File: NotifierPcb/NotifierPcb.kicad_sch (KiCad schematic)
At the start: 29 parts, among them IC1 CD4067BEE4, IC2 ESP32-WROOM-32E__8MB_, J1 RC_433_MHZ_RF, J2 UART_Conn, J3 Power_Conn, U1 HT75xx-1-SOT89

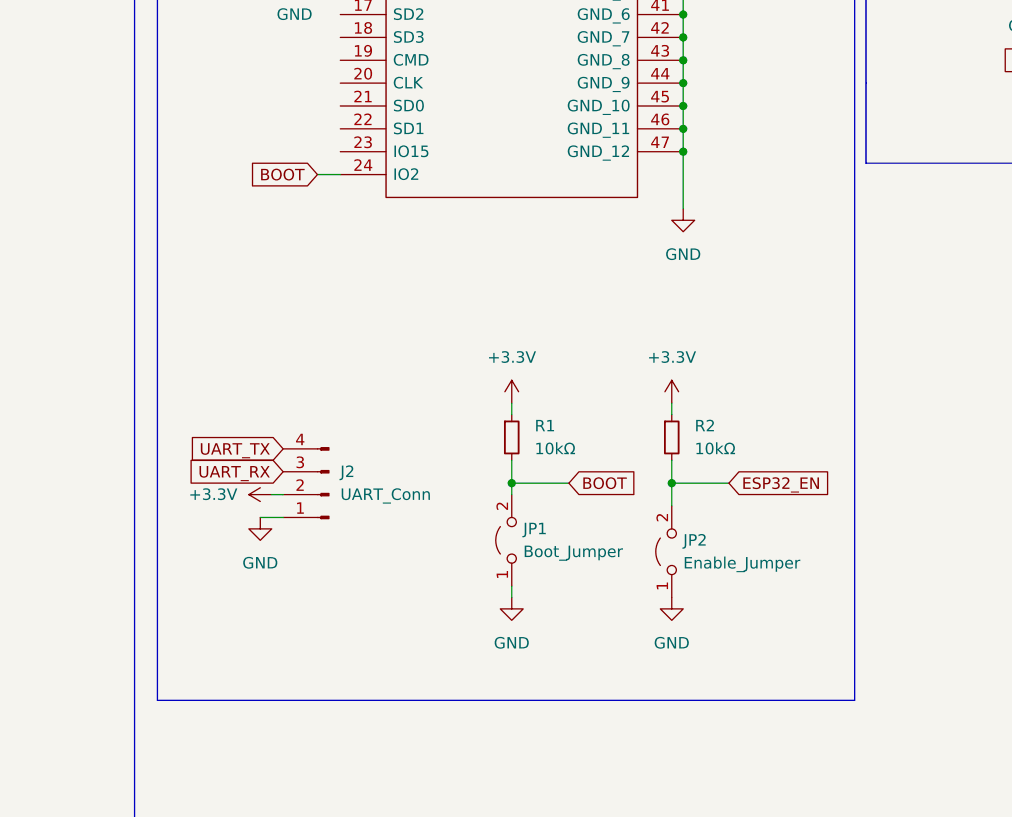
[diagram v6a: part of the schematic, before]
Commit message: fixing strapping pins for download mode
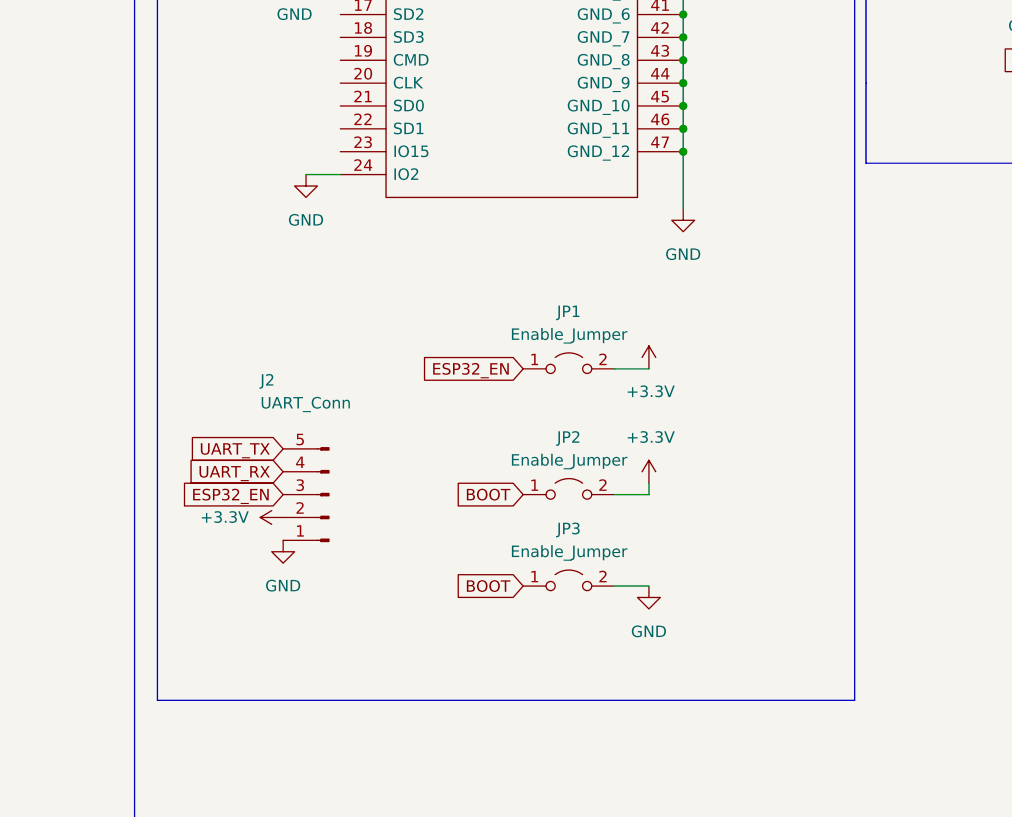
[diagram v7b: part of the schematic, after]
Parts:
- removed J2: UART_Conn, Connector_PinHeader_2.54mm:PinHeader_1x04_P2.54mm_Vertical, symbol Connector:Conn_01x04_Male
- removed JP1: Boot_Jumper, Connector_PinHeader_2.54mm:PinHeader_1x02_P2.54mm_Vertical, symbol Jumper:Jumper_2_Open
- removed R1, R2: 10kΩ, Resistor_THT:R_Axial_DIN0204_L3.6mm_D1.6mm_P2.54mm_Vertical, symbol Device:R_Small
- added J2: UART_Conn, symbol Connector:Conn_01x05_Male
- added JP2, JP3: Enable_Jumper, Connector_PinHeader_2.54mm:PinHeader_1x02_P2.54mm_Vertical, symbol Jumper:Jumper_2_Open
- renumbered JP2 to JP1
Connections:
- net +3.3V: now also JP1.2 (B), J2.2 (Pin_2), JP2.2 (B)
- net BOOT: now also JP2.1 (A), JP3.1 (A); no longer IC2.24 (IO2)
- net ESP32_EN: now also JP1.1 (A), J2.3 (Pin_3); no longer JP1.2 (B)
- net GND: now also IC2.24 (IO2), J2.1 (Pin_1), JP3.2 (B); no longer JP1.1 (A)
- net UART_RX: now also J2.4 (Pin_4)
- net UART_TX: now also J2.5 (Pin_5)
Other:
- moved on the sheet: JP1

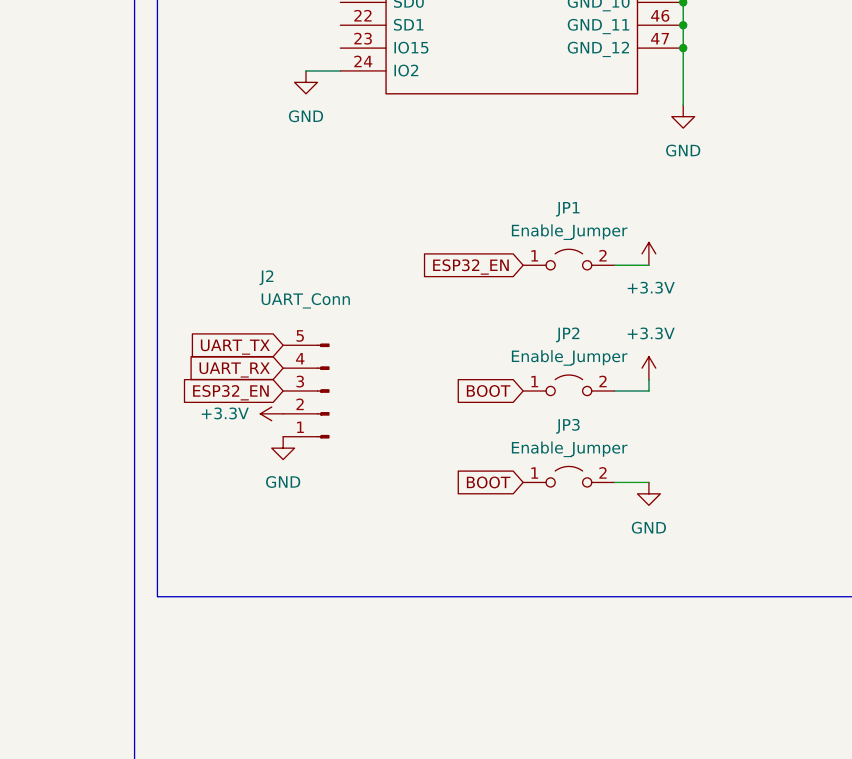
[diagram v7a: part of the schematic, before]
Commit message: new configuratio for boot pins selection
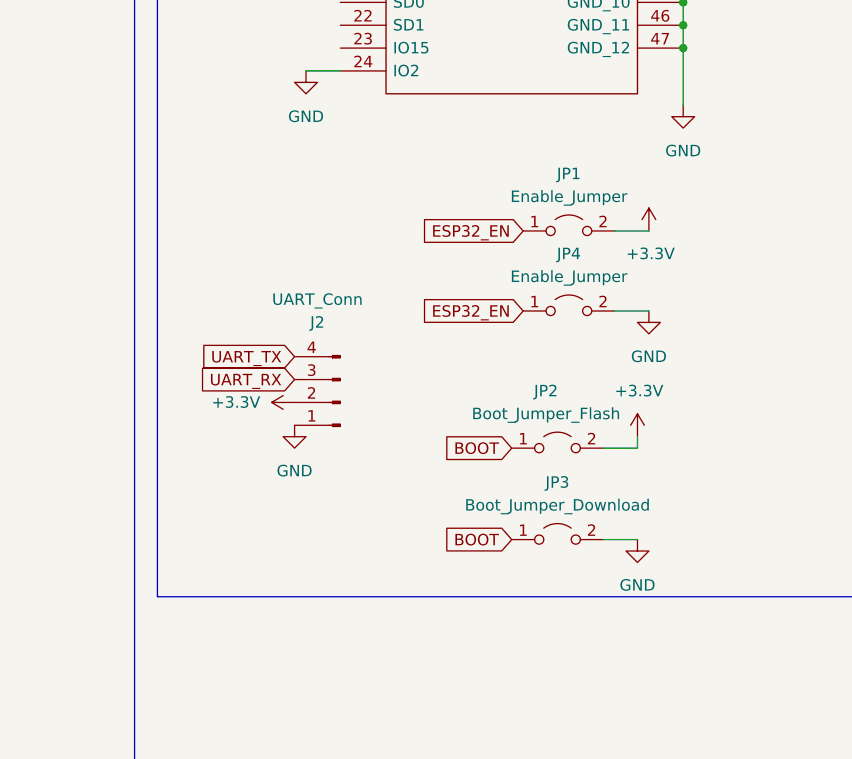
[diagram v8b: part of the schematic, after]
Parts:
- removed J2: UART_Conn, symbol Connector:Conn_01x05_Male
- added J2: UART_Conn, Connector_PinHeader_2.54mm:PinHeader_1x04_P2.54mm_Vertical, symbol Connector:Conn_01x04_Male
- added JP4: Enable_Jumper, Connector_PinHeader_2.54mm:PinHeader_1x02_P2.54mm_Vertical, symbol Jumper:Jumper_2_Open
- IC1: footprint (none) -> CD4067:DIP1080W53P254L3104H508Q24N
- IC2: footprint ESP32WROOM32E8MB -> ESP32-WROOM:ESP32WROOM32E8MB
- JP2: value Enable_Jumper -> Boot_Jumper_Flash
- JP3: value Enable_Jumper -> Boot_Jumper_Download
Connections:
- net +3.3V: now also J2.2 (Pin_2)
- net ESP32_EN: now also JP4.1 (A)
- net GND: now also J2.1 (Pin_1), JP4.2 (B)
- net UART_RX: now also J2.3 (Pin_3)
- net UART_TX: now also J2.4 (Pin_4)
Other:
- moved on the sheet: JP1, JP2, JP3
